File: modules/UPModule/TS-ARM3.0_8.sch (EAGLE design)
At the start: 80 parts, among them IC1 LPC1115, IC100 BD9G101, P1 , P10 , P11 , P12 , P13 , P14 , P2 , P3 , P4 , P5 , P6 , P7 , P8 , P9 , T1 BC856, T2 BCP52, T3 BC847, X1 EIB

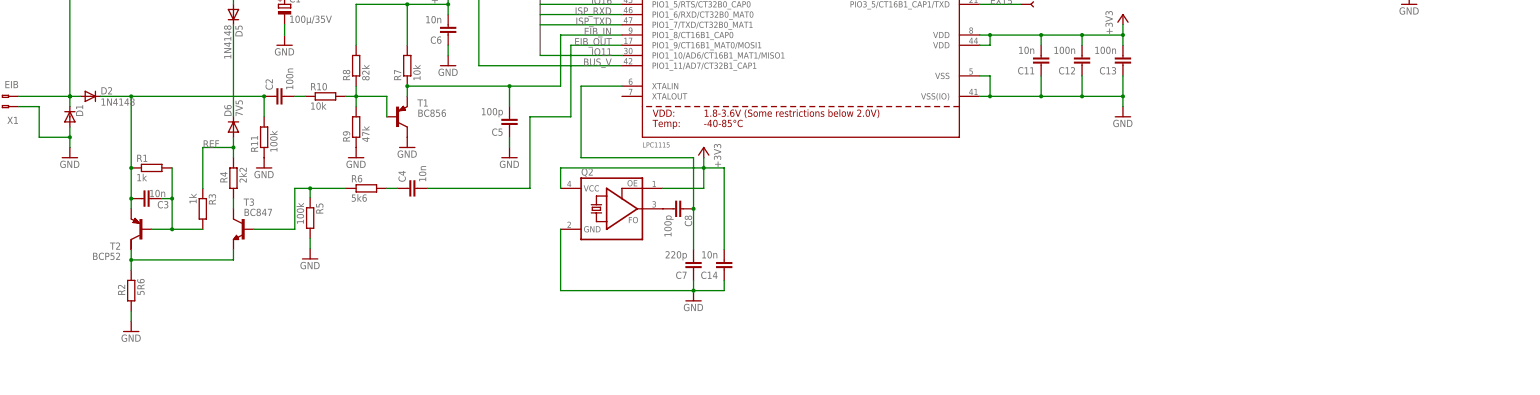
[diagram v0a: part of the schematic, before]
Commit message: text placement optimized; Pin description added
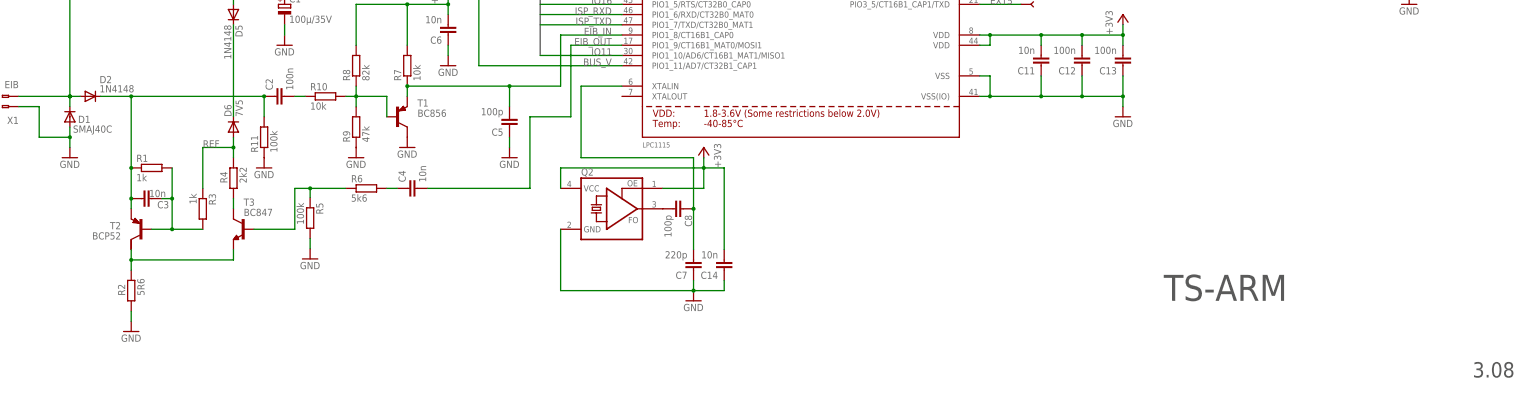
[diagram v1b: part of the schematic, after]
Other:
- note added: "3.08"
- note added: "TS-ARM"
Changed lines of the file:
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@@
 <?xml version="1.0" encoding="utf-8"?>
 <!DOCTYPE eagle SYSTEM "eagle.dtd">
-<eagle version="7.4.0">
+<eagle version="6.3">
 <drawing>
 <settings>
@@
 <layer number="2" name="Route2" color="1" fill="3" visible="no" active="no"/>
 <layer number="3" name="Route3" color="4" fill="3" visible="no" active="no"/>
+<layer number="4" name="Route4" color="1" fill="4" visible="no" active="no"/>
+<layer number="5" name="Route5" color="4" fill="4" visible="no" active="no"/>
+<layer number="6" name="Route6" color="1" fill="8" visible="no" active="no"/>
+<layer number="7" name="Route7" color="4" fill="8" visible="no" active="no"/>
+<layer number="8" name="Route8" color="1" fill="2" visible="no" active="no"/>
+<layer number="9" name="Route9" color="4" fill="2" visible="no" active="no"/>
+<layer number="10" name="Route10" color="1" fill="7" visible="no" active="no"/>
+<layer number="11" name="Route11" color="4" fill="7" visible="no" active="no"/>
+<layer number="12" name="Route12" color="1" fill="5" visible="no" active="no"/>
+<layer number="13" name="Route13" color="4" fill="5" visible="no" active="no"/>
 <layer number="14" name="Route14" color="1" fill="6" visible="no" active="no"/>
 <layer number="15" name="Route15" color="4" fill="6" visible="no" active="no"/>
@@
 <part name="C8" library="rcl" deviceset="C-EU" device="C1206" value="100p"/>
 <part name="C14" library="rcl" deviceset="C-EU" device="C1206" value="10n"/>
+<part name="FRAME1" library="frames" deviceset="DINA3_L" device=""/>
 </parts>
 <sheets>
@@
 <text x="-35.56" y="137.16" size="1.778" layer="91">Rechnerischer Wert C101: ca. 300nF</text>
 <text x="68.58" y="88.9" size="1.778" layer="91">I2C PullUps</text>
+<text x="88.9" y="-86.36" size="6.4516" layer="97">TS-ARM</text>
+<text x="165.608" y="-105.41" size="3.81" layer="97">3.08</text>
 </plain>
 <instances>
@@
 <instance part="P+6" gate="G$1" x="-58.42" y="55.88" rot="MR0"/>
 <instance part="GND25" gate="1" x="-73.66" y="22.86"/>
-<instance part="D2" gate="G$1" x="-177.8" y="-35.56">
+<instance part="D2" gate="G$1" x="-177.8" y="-35.56" smashed="yes">
 <attribute name="REICHELT" x="-177.8" y="-35.56" size="1.778" layer="96" display="off"/>
+<attribute name="NAME" x="-175.514" y="-32.2834" size="1.778" layer="95"/>
+<attribute name="VALUE" x="-175.514" y="-34.5694" size="1.778" layer="96"/>
 </instance>
 <instance part="R13" gate="G$1" x="-106.68" y="38.1" rot="R270">
@@
 </instance>
 <instance part="T2" gate="G$1" x="-165.1" y="-68.58" smashed="yes" rot="MR0">
-<attribute name="NAME" x="-170.18" y="-73.66" size="1.778" layer="95" rot="MR0"/>
-<attribute name="VALUE" x="-170.18" y="-76.2" size="1.778" layer="96" rot="MR0"/>
+<attribute name="NAME" x="-170.18" y="-68.58" size="1.778" layer="95" rot="MR0"/>
+<attribute name="VALUE" x="-170.18" y="-71.12" size="1.778" layer="96" rot="MR0"/>
 <attribute name="REICHELT" x="-165.1" y="-68.58" size="1.778" layer="96" rot="MR0" display="off"/>
 </instance>
@@
 <instance part="GND1" gate="1" x="-182.88" y="-50.8"/>
 <instance part="D1" gate="G$1" x="-182.88" y="-40.64" smashed="yes" rot="R90">
-<attribute name="NAME" x="-179.578" y="-40.64" size="1.778" layer="95" rot="R90"/>
+<attribute name="NAME" x="-180.848" y="-42.164" size="1.778" layer="95"/>
+<attribute name="VALUE" x="-182.118" y="-44.577" size="1.778" layer="96"/>
 </instance>
 <instance part="P+1" gate="G$1" x="78.74" y="-15.24"/>
@@
 <instance part="C8" gate="G$1" x="-30.48" y="-63.5" rot="R270"/>
 <instance part="C14" gate="G$1" x="-20.32" y="-78.74" rot="R180"/>
+<instance part="FRAME1" gate="G$1" x="-210.82" y="-111.76"/>
+<instance part="FRAME1" gate="G$2" x="76.2" y="-111.76"/>
 </instances>
 <busses>
